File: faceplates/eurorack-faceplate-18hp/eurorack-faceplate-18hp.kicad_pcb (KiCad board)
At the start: 2 copper layers, 91.3 x 133.3 mm, 4 parts

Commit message: Moving mounting holes
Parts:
- moved REF** 2.52 mm to (86.2, 130.3)
- moved REF** 2.52 mm to (86.2, 3.00)
- moved REF** 2.42 mm to (5.08, 130.3)
- moved REF** 2.42 mm to (5.08, 3.00)
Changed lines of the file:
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@@
   (net 0 "")
   (footprint "MountingHole:MountingHole_3.2mm_M3" (layer "F.Cu")
-    (at 7.5 130.35)
+    (at 5.08 130.35)
     (descr "Mounting Hole 3.2mm, no annular, M3")
     (tags "mounting hole 3.2mm no annular m3")
@@
   )
   (footprint "MountingHole:MountingHole_3.2mm_M3" (layer "F.Cu")
-    (at 83.7 130.35)
+    (at 86.22 130.35)
     (descr "Mounting Hole 3.2mm, no annular, M3")
     (tags "mounting hole 3.2mm no annular m3")
@@
   )
   (footprint "MountingHole:MountingHole_3.2mm_M3" (layer "F.Cu")
-    (at 83.7 3)
+    (at 86.22 3)
     (descr "Mounting Hole 3.2mm, no annular, M3")
     (tags "mounting hole 3.2mm no annular m3")
@@
   )
   (footprint "MountingHole:MountingHole_3.2mm_M3" (layer "F.Cu")
-    (at 7.5 3)
+    (at 5.08 3)
     (descr "Mounting Hole 3.2mm, no annular, M3")
     (tags "mounting hole 3.2mm no annular m3")
@@
   (gr_line (start 0 0) (end 91.3 0) (layer "Edge.Cuts") (width 0.1))
   (gr_line (start 91.3 133.35) (end 0 133.35) (layer "Edge.Cuts") (width 0.1))
+  (dimension (type aligned) (layer "User.1")
+    (pts (xy 5.08 3) (xy 0 3))
+    (height 8)
+    (gr_text "5.0800 mm" (at 2.54 -6.15) (layer "User.1")
+      (effects (font (size 1 1) (thickness 0.15)))
+    )
+    (format (units 3) (units_format 1) (precision 4))
+    (style (thickness 0.1) (arrow_length 1.27) (text_position_mode 0) (extension_height 0.58642) (extension_offset 0.5) keep_text_aligned)
+  )
 )

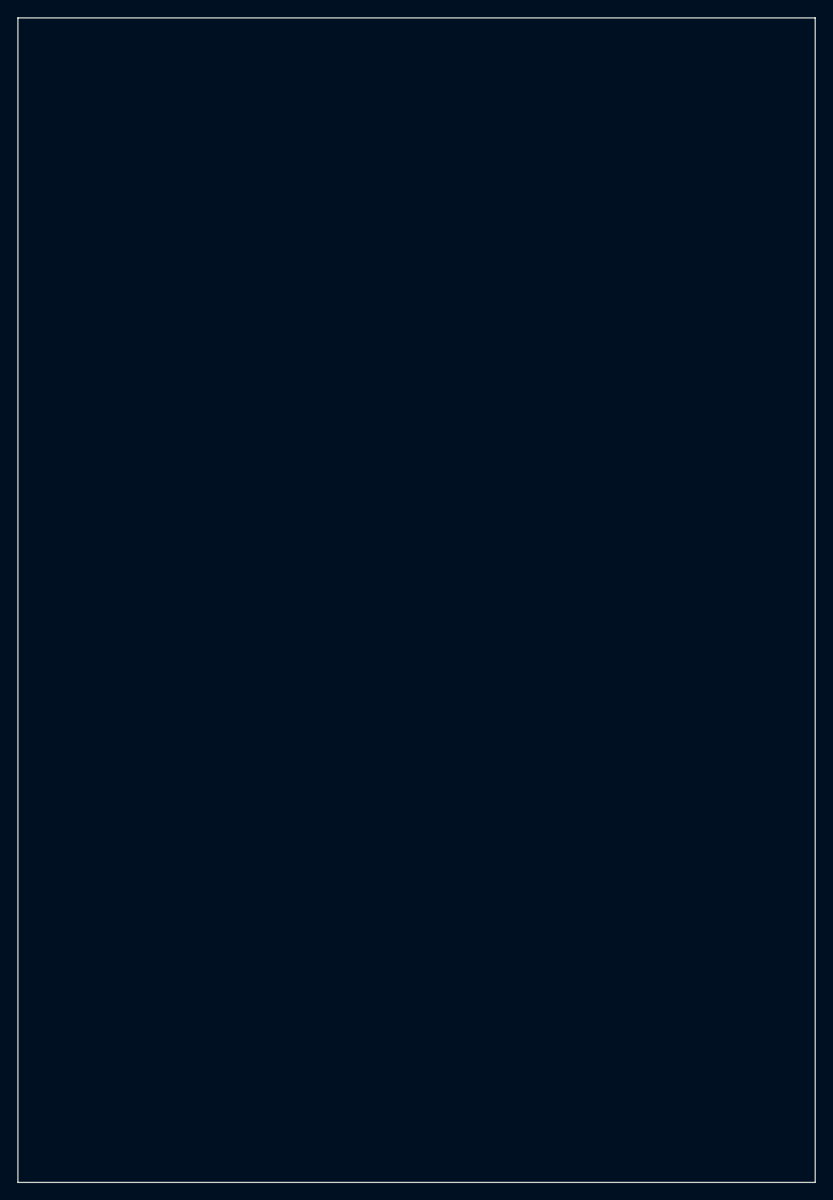
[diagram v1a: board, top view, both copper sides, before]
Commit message: Correcting panel height
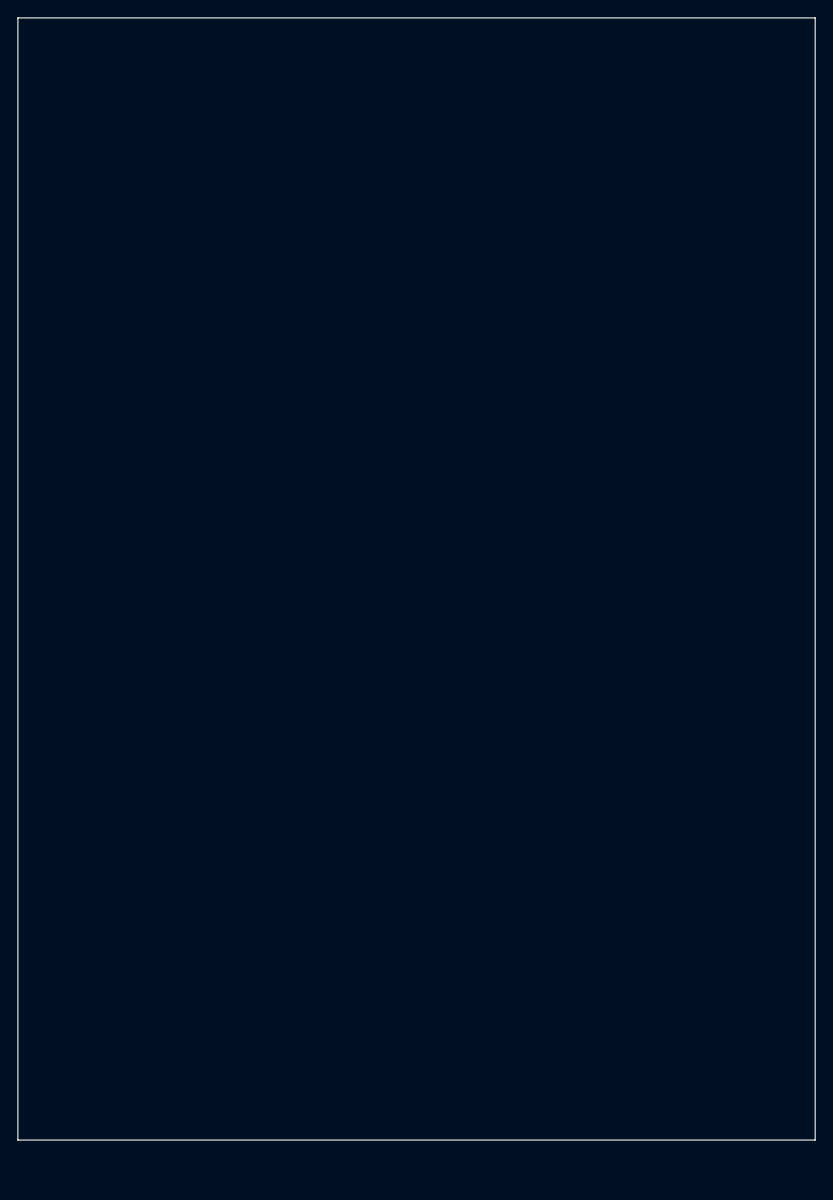
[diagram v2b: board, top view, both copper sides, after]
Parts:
- moved REF** 4.85 mm to (5.08, 125.5)
- moved REF** 4.85 mm to (86.2, 125.5)
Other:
- board size 91.3 x 133.3 mm -> 91.3 x 128.5 mm
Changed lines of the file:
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@@
   (net 0 "")
   (footprint "MountingHole:MountingHole_3.2mm_M3" (layer "F.Cu")
-    (at 5.08 130.35)
+    (at 5.08 125.5)
     (descr "Mounting Hole 3.2mm, no annular, M3")
     (tags "mounting hole 3.2mm no annular m3")
@@
   )
   (footprint "MountingHole:MountingHole_3.2mm_M3" (layer "F.Cu")
-    (at 86.22 130.35)
+    (at 86.22 125.5)
     (descr "Mounting Hole 3.2mm, no annular, M3")
     (tags "mounting hole 3.2mm no annular m3")
@@
     (pad "" np_thru_hole oval locked (at 0 0) (size 7 3.2) (drill oval 7 3.2) (layers F&B.Cu *.Mask))
   )
-  (gr_line (start 91.3 0) (end 91.3 133.35) (layer "Edge.Cuts") (width 0.1))
-  (gr_line (start 0 133.35) (end 0 0) (layer "Edge.Cuts") (width 0.1))
+  (gr_line (start 91.3 0) (end 91.3 128.5) (layer "Edge.Cuts") (width 0.1))
+  (gr_line (start 0 128.5) (end 0 0) (layer "Edge.Cuts") (width 0.1))
   (gr_line (start 0 0) (end 91.3 0) (layer "Edge.Cuts") (width 0.1))
-  (gr_line (start 91.3 133.35) (end 0 133.35) (layer "Edge.Cuts") (width 0.1))
+  (gr_line (start 91.3 128.5) (end 0 128.5) (layer "Edge.Cuts") (width 0.1))
   (dimension (type aligned) (layer "User.1")
     (pts (xy 5.08 3) (xy 0 3))
